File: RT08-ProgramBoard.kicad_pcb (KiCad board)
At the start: 2 copper layers, 190.5 x 149.9 mm, 313 parts, among them J1 PWR/Addr, J2 Inst-1, J3 Inst-2, J4 Data-1, J5 Data-2, J6 Inst-1, J7 Inst-2, J8 Data-1, J9 Data-2

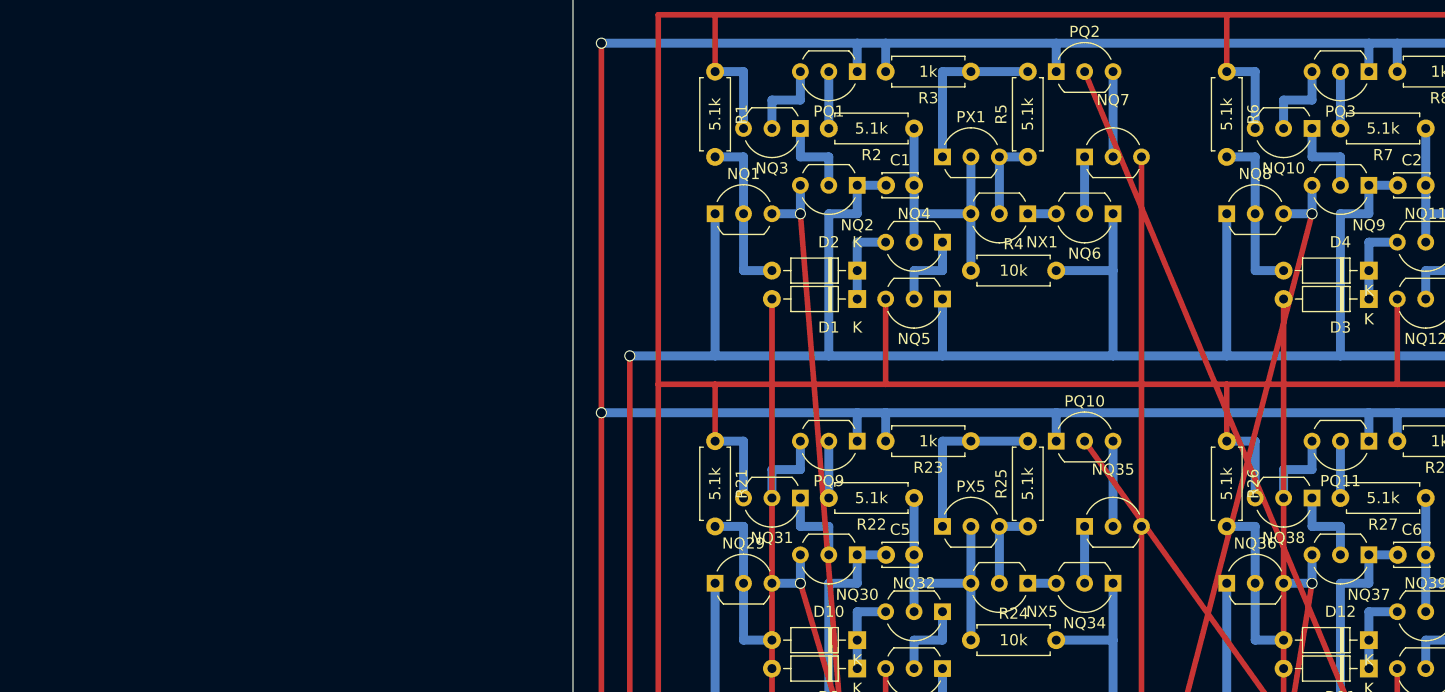
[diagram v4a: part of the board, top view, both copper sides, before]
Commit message: Adding one more parts per bit, editing PCB
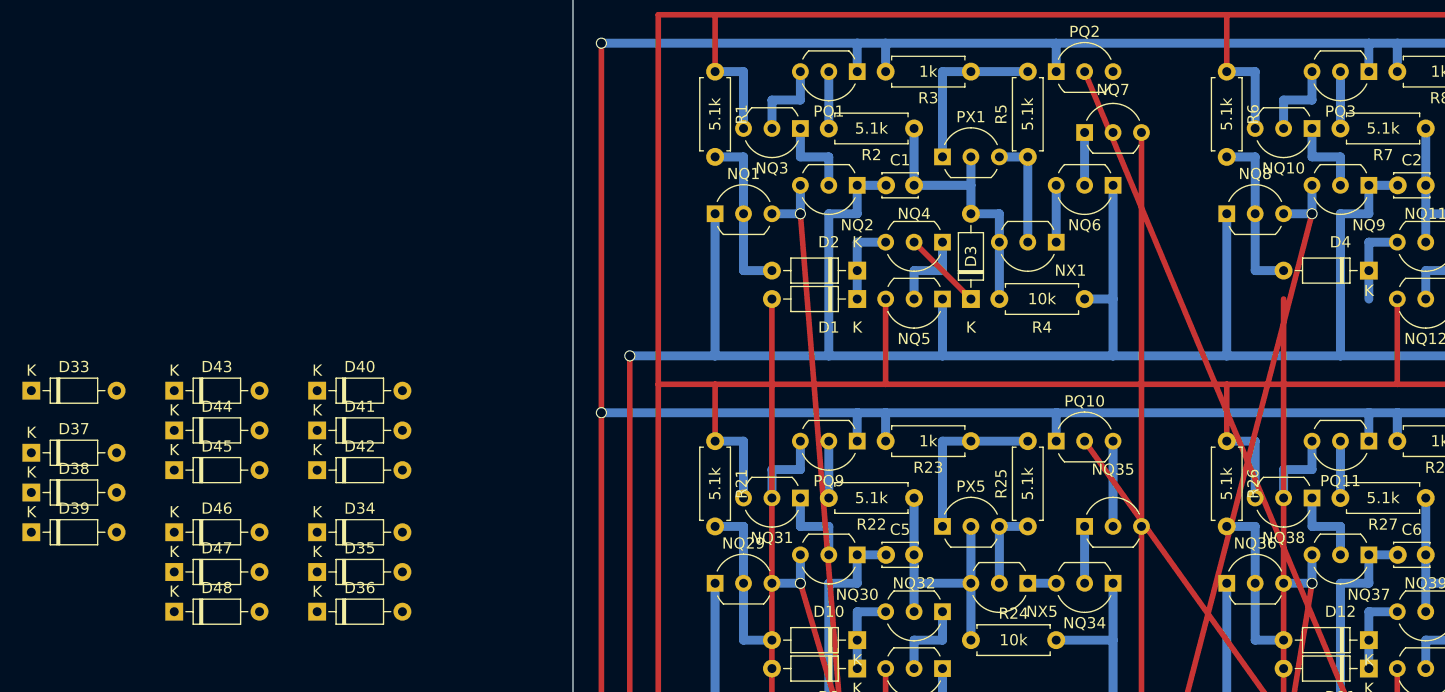
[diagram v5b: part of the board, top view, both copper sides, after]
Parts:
- added D33: Schottky, Diode_THT:D_DO-35_SOD27_P7.62mm_Horizontal, F.Cu at (-20.5, 53.9)
- added D34: Schottky, Diode_THT:D_DO-35_SOD27_P7.62mm_Horizontal, F.Cu at (5.08, 66.6)
- added D35: Schottky, Diode_THT:D_DO-35_SOD27_P7.62mm_Horizontal, F.Cu at (5.08, 70.1)
- added D36: Schottky, Diode_THT:D_DO-35_SOD27_P7.62mm_Horizontal, F.Cu at (5.08, 73.7)
- added D37: Schottky, Diode_THT:D_DO-35_SOD27_P7.62mm_Horizontal, F.Cu at (-20.5, 59.5)
- added D38: Schottky, Diode_THT:D_DO-35_SOD27_P7.62mm_Horizontal, F.Cu at (-20.5, 63.0)
- added D39: Schottky, Diode_THT:D_DO-35_SOD27_P7.62mm_Horizontal, F.Cu at (-20.5, 66.6)
- added D40: Schottky, Diode_THT:D_DO-35_SOD27_P7.62mm_Horizontal, F.Cu at (5.08, 53.9)
- added D41: Schottky, Diode_THT:D_DO-35_SOD27_P7.62mm_Horizontal, F.Cu at (5.08, 57.5)
- added D42: Schottky, Diode_THT:D_DO-35_SOD27_P7.62mm_Horizontal, F.Cu at (5.08, 61.0)
- added D43: Schottky, Diode_THT:D_DO-35_SOD27_P7.62mm_Horizontal, F.Cu at (-7.69, 53.9)
- added D44: Schottky, Diode_THT:D_DO-35_SOD27_P7.62mm_Horizontal, F.Cu at (-7.69, 57.5)
- added D45: Schottky, Diode_THT:D_DO-35_SOD27_P7.62mm_Horizontal, F.Cu at (-7.69, 61.0)
- added D46: Schottky, Diode_THT:D_DO-35_SOD27_P7.62mm_Horizontal, F.Cu at (-7.69, 66.6)
- added D47: Schottky, Diode_THT:D_DO-35_SOD27_P7.62mm_Horizontal, F.Cu at (-7.69, 70.1)
- added D48: Schottky, Diode_THT:D_DO-35_SOD27_P7.62mm_Horizontal, F.Cu at (-7.69, 73.7)
- moved D3 35.6 mm to (63.5, 45.7), turned to 90 degrees
- moved NX1 3.59 mm to (71.1, 40.6)
- moved R4 3.59 mm to (66.0, 45.7)
- moved NQ6 2.54 mm to (76.2, 35.6)
- moved NQ7 2.18 mm to (73.7, 30.8)
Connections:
- C1 pad 2: Net-(NQ4-C) -> Net-(D3-A)
- C10 pad 2: Net-(NQ67-C) -> Net-(D30-A)
- C11 pad 2: Net-(NQ74-C) -> Net-(D33-A)
- C12 pad 2: Net-(NQ81-C) -> Net-(D36-A)
- C13 pad 2: Net-(NQ88-C) -> Net-(D39-A)
- C14 pad 2: Net-(NQ95-C) -> Net-(D42-A)
- C15 pad 2: Net-(NQ102-C) -> Net-(D45-A)
- C16 pad 2: Net-(NQ109-C) -> Net-(D48-A)
- C2 pad 2: Net-(NQ11-C) -> Net-(D6-A)
- C3 pad 2: Net-(NQ18-C) -> Net-(D9-A)
- C4 pad 2: Net-(NQ25-C) -> Net-(D12-A)
- C5 pad 2: Net-(NQ32-C) -> Net-(D15-A)
- C6 pad 2: Net-(NQ39-C) -> Net-(D18-A)
- C7 pad 2: Net-(NQ46-C) -> Net-(D21-A)
- C8 pad 2: Net-(NQ53-C) -> Net-(D24-A)
- C9 pad 2: Net-(NQ60-C) -> Net-(D27-A)
- D10 pad 2: Net-(D10-A) -> /Rst
- D11 pad 1: Net-(D11-K) -> Net-(D10-K)
- D11 pad 2: /Rst -> Net-(D11-A)
- D12 pad 1: Net-(D11-K) -> Net-(D12-K)
- D15 pad 2: /Rst -> Net-(D15-A)
- D16 pad 1: Net-(D15-K) -> Net-(D16-K)
- D16 pad 2: Net-(D16-A) -> /Rst
- D17 pad 1: Net-(D17-K) -> Net-(D16-K)
- D17 pad 2: /Rst -> Net-(D17-A)
- D18 pad 1: Net-(D17-K) -> Net-(D18-K)
- D21 pad 2: /Rst -> Net-(D21-A)
- D22 pad 1: Net-(D21-K) -> Net-(D22-K)
- D22 pad 2: Net-(D22-A) -> /Rst
- D23 pad 1: Net-(D23-K) -> Net-(D22-K)
- D23 pad 2: /Rst -> Net-(D23-A)
- D24 pad 1: Net-(D23-K) -> Net-(D24-K)
- D27 pad 2: /Rst -> Net-(D27-A)
- D28 pad 1: Net-(D27-K) -> Net-(D28-K)
- D28 pad 2: Net-(D28-A) -> /Rst
- D29 pad 1: Net-(D29-K) -> Net-(D28-K)
- D29 pad 2: /Rst -> Net-(D29-A)
- D3 pad 2: /Rst -> Net-(D3-A)
- D30 pad 1: Net-(D29-K) -> Net-(D30-K)
- D4 pad 1: Net-(D3-K) -> Net-(D4-K)
- D4 pad 2: Net-(D4-A) -> /Rst
- D5 pad 1: Net-(D5-K) -> Net-(D4-K)
- D5 pad 2: /Rst -> Net-(D5-A)
- D6 pad 1: Net-(D5-K) -> Net-(D6-K)
- D9 pad 1: Net-(D10-K) -> Net-(D9-K)
- D9 pad 2: /Rst -> Net-(D9-A)
- NQ102 pad 2: Net-(NQ102-C) -> Net-(D45-K)
- NQ102 pad 3: Net-(D29-K) -> Net-(D43-K)
- NQ106 pad 2: Net-(D32-A) -> Net-(D47-A)
- NQ109 pad 2: Net-(NQ109-C) -> Net-(D48-K)
- NQ109 pad 3: Net-(D31-K) -> Net-(D46-K)
- NQ11 pad 2: Net-(NQ11-C) -> Net-(D6-K)
- NQ11 pad 3: Net-(D3-K) -> Net-(D4-K)
- NQ15 pad 2: Net-(D6-A) -> Net-(D8-A)
- NQ18 pad 2: Net-(NQ18-C) -> Net-(D9-K)
- NQ18 pad 3: Net-(D5-K) -> Net-(D7-K)
- NQ22 pad 2: Net-(D8-A) -> Net-(D11-A)
- NQ25 pad 2: Net-(NQ25-C) -> Net-(D12-K)
- NQ25 pad 3: Net-(D7-K) -> Net-(D10-K)
- NQ29 pad 2: Net-(D10-A) -> Net-(D14-A)
- NQ32 pad 2: Net-(NQ32-C) -> Net-(D15-K)
- NQ32 pad 3: Net-(D10-K) -> Net-(D13-K)
- NQ36 pad 2: Net-(D12-A) -> Net-(D17-A)
- NQ39 pad 2: Net-(NQ39-C) -> Net-(D18-K)
- NQ39 pad 3: Net-(D11-K) -> Net-(D16-K)
- NQ4 pad 2: Net-(NQ4-C) -> Net-(D3-K)
- NQ43 pad 2: Net-(D14-A) -> Net-(D20-A)
- NQ46 pad 2: Net-(NQ46-C) -> Net-(D21-K)
- NQ46 pad 3: Net-(D13-K) -> Net-(D19-K)
- NQ50 pad 2: Net-(D16-A) -> Net-(D23-A)
- NQ53 pad 2: Net-(NQ53-C) -> Net-(D24-K)
- NQ53 pad 3: Net-(D15-K) -> Net-(D22-K)
- NQ57 pad 2: Net-(D18-A) -> Net-(D26-A)
- NQ60 pad 2: Net-(NQ60-C) -> Net-(D27-K)
- NQ60 pad 3: Net-(D17-K) -> Net-(D25-K)
- NQ64 pad 2: Net-(D20-A) -> Net-(D29-A)
- NQ67 pad 2: Net-(NQ67-C) -> Net-(D30-K)
- NQ67 pad 3: Net-(D19-K) -> Net-(D28-K)
- NQ71 pad 2: Net-(D22-A) -> Net-(D32-A)
- NQ74 pad 2: Net-(NQ74-C) -> Net-(D33-K)
- NQ74 pad 3: Net-(D21-K) -> Net-(D31-K)
- NQ78 pad 2: Net-(D24-A) -> Net-(D35-A)
- NQ8 pad 2: Net-(D4-A) -> Net-(D5-A)
- NQ81 pad 2: Net-(NQ81-C) -> Net-(D36-K)
- NQ81 pad 3: Net-(D23-K) -> Net-(D34-K)
- NQ85 pad 2: Net-(D26-A) -> Net-(D38-A)
- NQ88 pad 2: Net-(NQ88-C) -> Net-(D39-K)
- NQ88 pad 3: Net-(D25-K) -> Net-(D37-K)
- NQ92 pad 2: Net-(D28-A) -> Net-(D41-A)
- NQ95 pad 2: Net-(NQ95-C) -> Net-(D42-K)
- NQ95 pad 3: Net-(D27-K) -> Net-(D40-K)
- NQ99 pad 2: Net-(D30-A) -> Net-(D44-A)
- NX1 pad 3: Net-(NQ4-C) -> Net-(D3-A)
- NX10 pad 3: Net-(NQ67-C) -> Net-(D30-A)
- NX11 pad 3: Net-(NQ74-C) -> Net-(D33-A)
- NX12 pad 3: Net-(NQ81-C) -> Net-(D36-A)
- NX13 pad 3: Net-(NQ88-C) -> Net-(D39-A)
- NX14 pad 3: Net-(NQ95-C) -> Net-(D42-A)
- NX15 pad 3: Net-(NQ102-C) -> Net-(D45-A)
- NX16 pad 3: Net-(NQ109-C) -> Net-(D48-A)
- NX2 pad 3: Net-(NQ11-C) -> Net-(D6-A)
- NX3 pad 3: Net-(NQ18-C) -> Net-(D9-A)
- NX4 pad 3: Net-(NQ25-C) -> Net-(D12-A)
- NX5 pad 3: Net-(NQ32-C) -> Net-(D15-A)
- NX6 pad 3: Net-(NQ39-C) -> Net-(D18-A)
- NX7 pad 3: Net-(NQ46-C) -> Net-(D21-A)
- NX8 pad 3: Net-(NQ53-C) -> Net-(D24-A)
- NX9 pad 3: Net-(NQ60-C) -> Net-(D27-A)
- PX1 pad 2: Net-(NQ4-C) -> Net-(D3-A)
- PX10 pad 2: Net-(NQ67-C) -> Net-(D30-A)
- PX11 pad 2: Net-(NQ74-C) -> Net-(D33-A)
- PX12 pad 2: Net-(NQ81-C) -> Net-(D36-A)
- PX13 pad 2: Net-(NQ88-C) -> Net-(D39-A)
- PX14 pad 2: Net-(NQ95-C) -> Net-(D42-A)
- PX15 pad 2: Net-(NQ102-C) -> Net-(D45-A)
- PX16 pad 2: Net-(NQ109-C) -> Net-(D48-A)
- PX2 pad 2: Net-(NQ11-C) -> Net-(D6-A)
- PX3 pad 2: Net-(NQ18-C) -> Net-(D9-A)
- PX4 pad 2: Net-(NQ25-C) -> Net-(D12-A)
- PX5 pad 2: Net-(NQ32-C) -> Net-(D15-A)
- PX6 pad 2: Net-(NQ39-C) -> Net-(D18-A)
- PX7 pad 2: Net-(NQ46-C) -> Net-(D21-A)
- PX8 pad 2: Net-(NQ53-C) -> Net-(D24-A)
- PX9 pad 2: Net-(NQ60-C) -> Net-(D27-A)
- R11 pad 2: Net-(D6-A) -> Net-(D8-A)
- R12 pad 1: Net-(NQ18-C) -> Net-(D9-A)
- R14 pad 1: Net-(NQ18-C) -> Net-(D9-A)
- R16 pad 2: Net-(D8-A) -> Net-(D11-A)
- R17 pad 1: Net-(NQ25-C) -> Net-(D12-A)
- R19 pad 1: Net-(NQ25-C) -> Net-(D12-A)
- R2 pad 1: Net-(NQ4-C) -> Net-(D3-A)
- R21 pad 2: Net-(D10-A) -> Net-(D14-A)
- R22 pad 1: Net-(NQ32-C) -> Net-(D15-A)
- R24 pad 1: Net-(NQ32-C) -> Net-(D15-A)
- R26 pad 2: Net-(D12-A) -> Net-(D17-A)
- R27 pad 1: Net-(NQ39-C) -> Net-(D18-A)
- R29 pad 1: Net-(NQ39-C) -> Net-(D18-A)
- R31 pad 2: Net-(D14-A) -> Net-(D20-A)
- R32 pad 1: Net-(NQ46-C) -> Net-(D21-A)
- R34 pad 1: Net-(NQ46-C) -> Net-(D21-A)
- R36 pad 2: Net-(D16-A) -> Net-(D23-A)
- R37 pad 1: Net-(NQ53-C) -> Net-(D24-A)
- R39 pad 1: Net-(NQ53-C) -> Net-(D24-A)
- R4 pad 1: Net-(NQ4-C) -> Net-(D3-A)
- R41 pad 2: Net-(D18-A) -> Net-(D26-A)
- R42 pad 1: Net-(NQ60-C) -> Net-(D27-A)
- R44 pad 1: Net-(NQ60-C) -> Net-(D27-A)
- R46 pad 2: Net-(D20-A) -> Net-(D29-A)
- R47 pad 1: Net-(NQ67-C) -> Net-(D30-A)
- R49 pad 1: Net-(NQ67-C) -> Net-(D30-A)
- R51 pad 2: Net-(D22-A) -> Net-(D32-A)
- R52 pad 1: Net-(NQ74-C) -> Net-(D33-A)
- R54 pad 1: Net-(NQ74-C) -> Net-(D33-A)
- R56 pad 2: Net-(D24-A) -> Net-(D35-A)
- R57 pad 1: Net-(NQ81-C) -> Net-(D36-A)
- R59 pad 1: Net-(NQ81-C) -> Net-(D36-A)
- R6 pad 2: Net-(D4-A) -> Net-(D5-A)
- R61 pad 2: Net-(D26-A) -> Net-(D38-A)
- R62 pad 1: Net-(NQ88-C) -> Net-(D39-A)
- R64 pad 1: Net-(NQ88-C) -> Net-(D39-A)
- R66 pad 2: Net-(D28-A) -> Net-(D41-A)
- R67 pad 1: Net-(NQ95-C) -> Net-(D42-A)
- R69 pad 1: Net-(NQ95-C) -> Net-(D42-A)
- R7 pad 1: Net-(NQ11-C) -> Net-(D6-A)
- R71 pad 2: Net-(D30-A) -> Net-(D44-A)
- R72 pad 1: Net-(NQ102-C) -> Net-(D45-A)
- R74 pad 1: Net-(NQ102-C) -> Net-(D45-A)
- R76 pad 2: Net-(D32-A) -> Net-(D47-A)
- R77 pad 1: Net-(NQ109-C) -> Net-(D48-A)
- R79 pad 1: Net-(NQ109-C) -> Net-(D48-A)
- R9 pad 1: Net-(NQ11-C) -> Net-(D6-A)
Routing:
- net (no net): track 0.00 -> 337.8 mm
- net Net-(NQ67-C): track 25.4 -> 0.00 mm
- net Net-(NQ60-C): track 25.4 -> 0.00 mm
- net Net-(D3-A): track 0.00 -> 25.4 mm
- net Net-(NQ4-C): track 25.4 -> 0.00 mm
- net Net-(NQ11-C): track 25.4 -> 0.00 mm
- net Net-(NQ95-C): track 25.4 -> 0.00 mm
- net Net-(NQ88-C): track 25.4 -> 0.00 mm
- net Net-(NQ81-C): track 25.4 -> 0.00 mm
- net Net-(NQ74-C): track 25.4 -> 0.00 mm
- net Net-(NQ39-C): track 25.4 -> 0.00 mm
- net Net-(NQ32-C): track 25.4 -> 0.00 mm
- net Net-(D6-A): track 15.2 -> 40.6 mm
- net Net-(D18-A): track 15.2 -> 40.6 mm
- net Net-(D15-K): track 7.62 -> 33.0 mm
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
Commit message: Finished editing PCB
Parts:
- moved D48 220.2 mm to (200.7, 144.8), turned to 90 degrees
- moved D46 213.1 mm to (190.5, 144.8), turned to 180 degrees
- moved D47 210.9 mm to (190.5, 142.2), turned to 180 degrees
- moved D36 199.3 mm to (200.7, 111.8), turned to 90 degrees
- moved D34 190.8 mm to (190.5, 111.8), turned to 180 degrees
- moved D35 189.5 mm to (190.5, 109.2), turned to 180 degrees
- moved D33 184.7 mm to (154.9, 111.8), turned to 90 degrees
- moved D45 182.9 mm to (154.9, 144.8), turned to 90 degrees
- moved D43 177.5 mm to (144.8, 144.8), turned to 180 degrees
- moved D44 174.5 mm to (144.8, 142.2), turned to 180 degrees
- moved D10 140.5 mm to (190.5, 45.7)
- moved D42 133.7 mm to (109.2, 144.8), turned to 90 degrees
- moved D40 130.7 mm to (99.1, 144.8), turned to 180 degrees
- moved D15 127.0 mm to (63.5, 78.7), turned to 90 degrees
- moved D41 126.6 mm to (99.1, 142.2), turned to 180 degrees
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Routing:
- net (no net): track 337.8 -> 0.00 mm
- net Net-(D15-K): track 33.0 -> 0.00 mm
- net Net-(D42-A): track 0.00 -> 25.4 mm
- net Net-(D39-A): track 0.00 -> 25.4 mm
- net Net-(D27-A): track 0.00 -> 25.4 mm
- net Net-(D15-A): track 0.00 -> 25.4 mm
- net Net-(D48-A): track 0.00 -> 25.4 mm
- net Net-(D45-A): track 0.00 -> 25.4 mm
- net Net-(D36-A): track 0.00 -> 25.4 mm
- net Net-(D33-A): track 0.00 -> 25.4 mm
- net Net-(D9-A): track 0.00 -> 25.4 mm
- net Net-(D21-A): track 0.00 -> 25.4 mm
- net Net-(D12-A): track 40.6 -> 25.4 mm
- net Net-(D5-A): track 0.00 -> 15.2 mm
- net Net-(D41-A): track 0.00 -> 15.2 mm
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
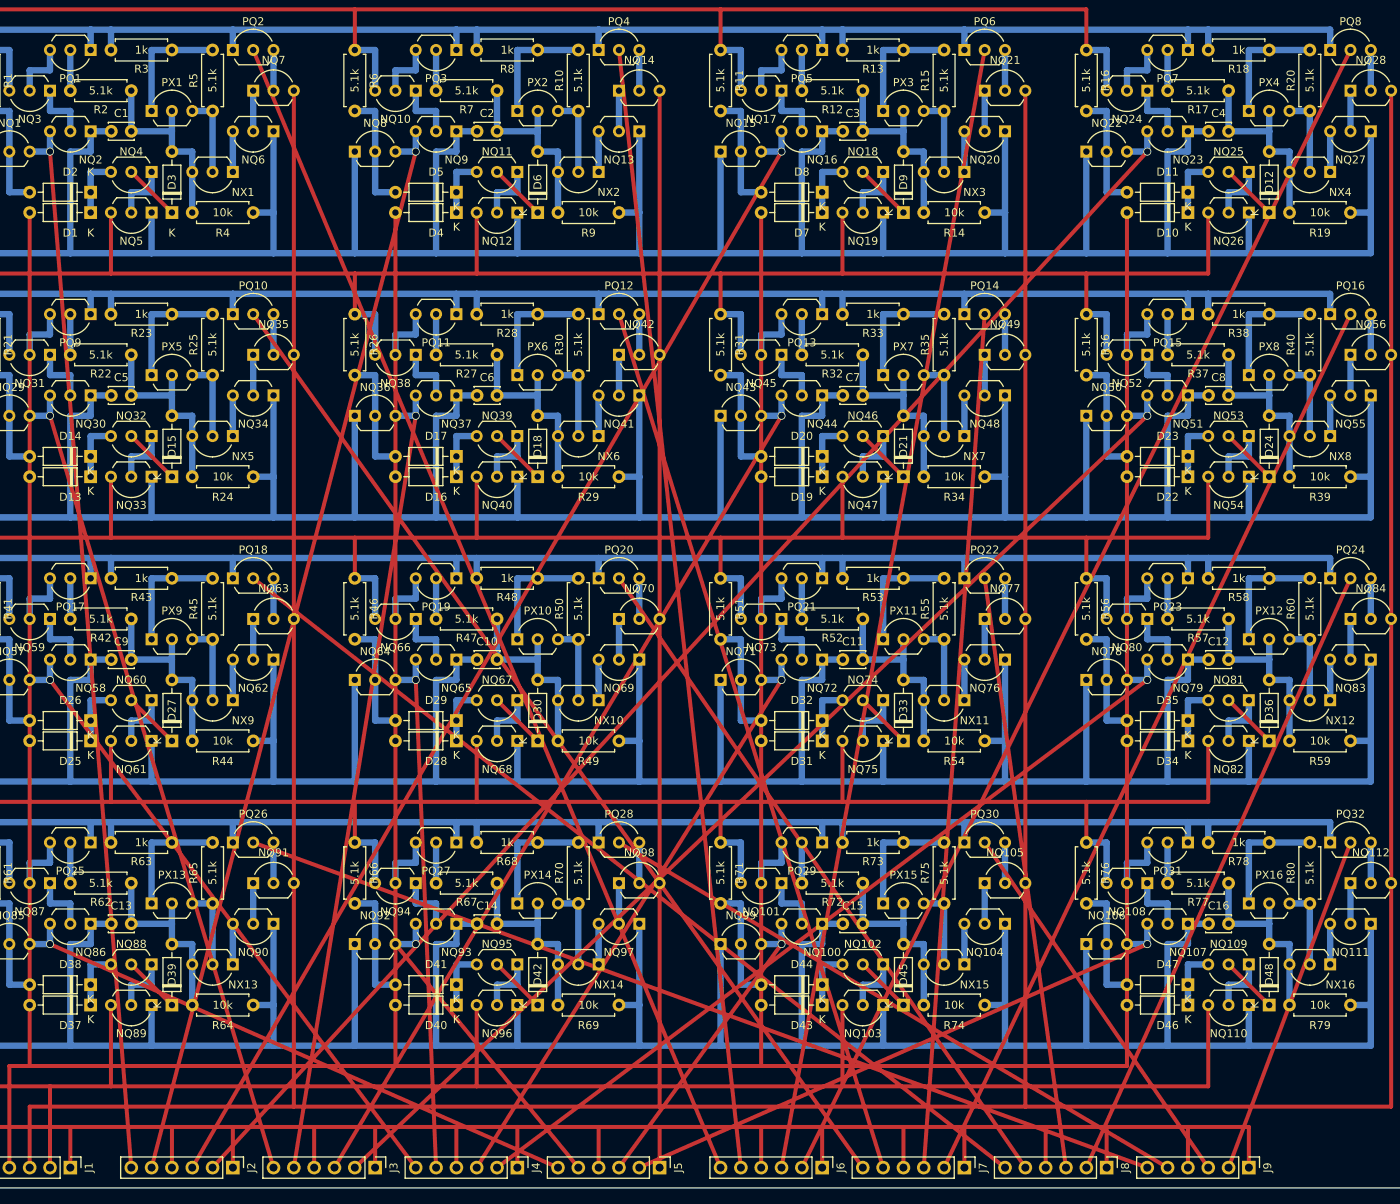
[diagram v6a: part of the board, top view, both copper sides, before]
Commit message: Merged In/Out pins to one pin groups!
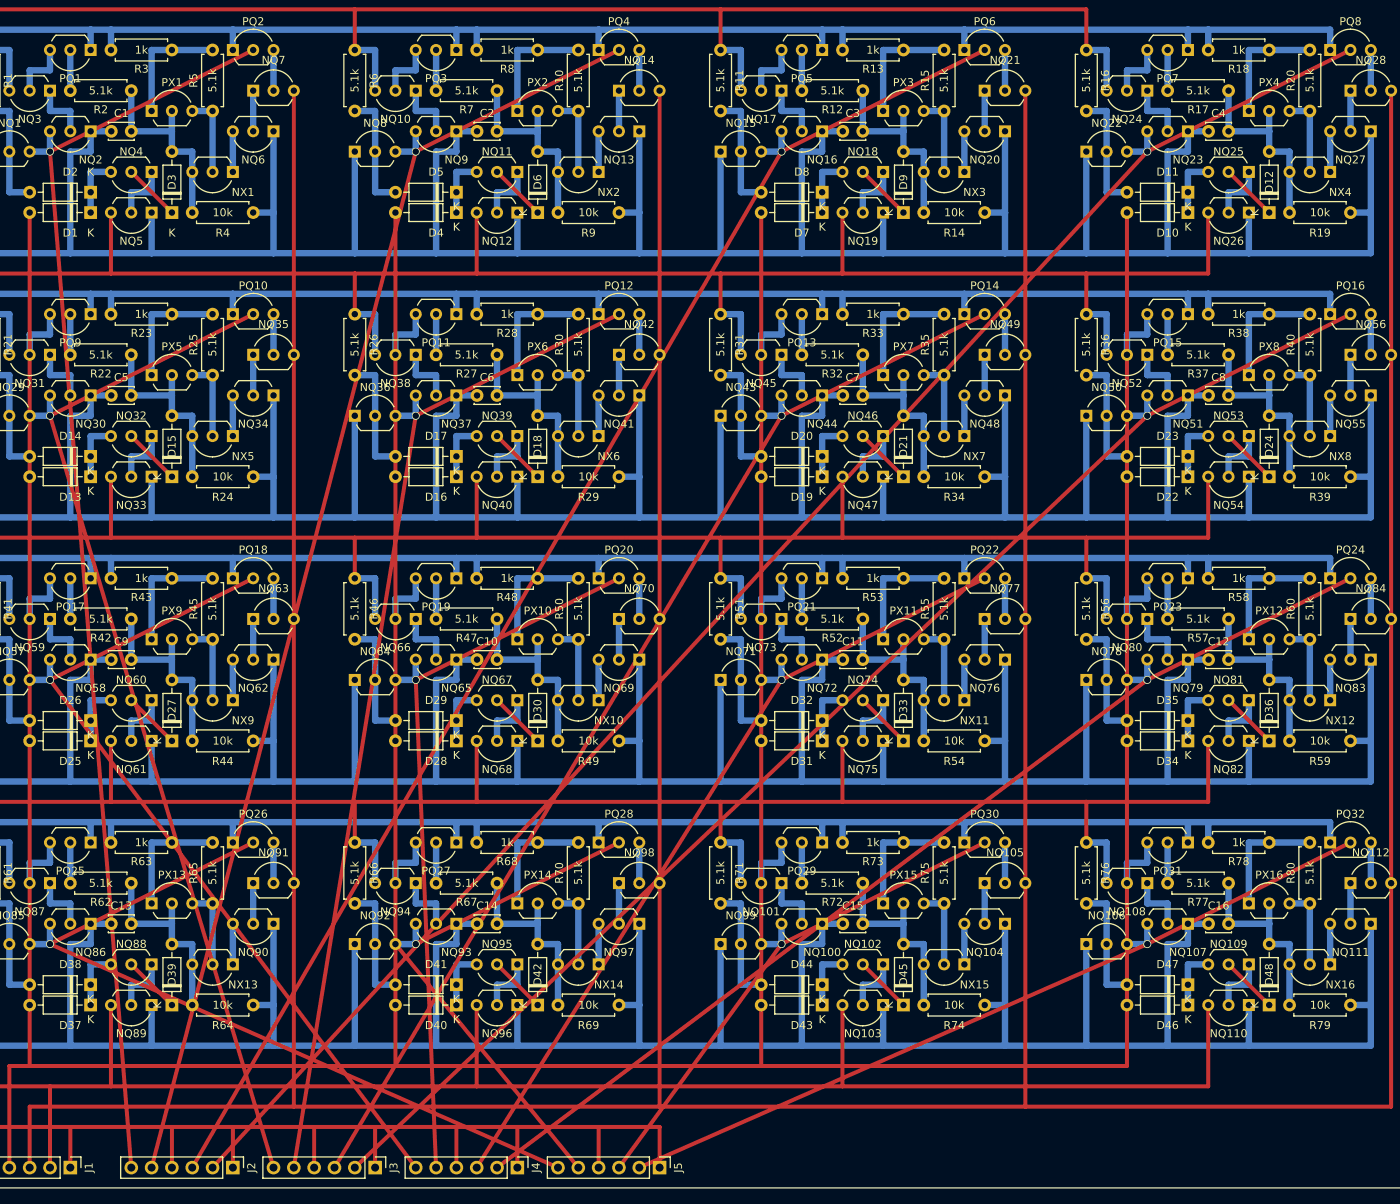
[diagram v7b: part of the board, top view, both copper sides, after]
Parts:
- removed J6: Inst-1, Connector_PinHeader_2.54mm:PinHeader_1x06_P2.54mm_Vertical
- removed J7: Inst-2, Connector_PinHeader_2.54mm:PinHeader_1x06_P2.54mm_Vertical
- removed J8: Data-1, Connector_PinHeader_2.54mm:PinHeader_1x06_P2.54mm_Vertical
- removed J9: Data-2, Connector_PinHeader_2.54mm:PinHeader_1x06_P2.54mm_Vertical
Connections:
- PQ10 pad 2: /P4 -> /D4
- PQ12 pad 2: /P5 -> /D5
- PQ14 pad 2: /P6 -> /D6
- PQ16 pad 2: /P7 -> /D7
- PQ18 pad 2: /P8 -> /D8
- PQ2 pad 2: /P0 -> /D0
- PQ20 pad 2: /P9 -> /D9
- PQ22 pad 2: /P10 -> /D10
- PQ24 pad 2: /P11 -> /D11
- PQ26 pad 2: /P12 -> /D12
- PQ28 pad 2: /P13 -> /D13
- PQ30 pad 2: /P14 -> /D14
- PQ32 pad 2: /P15 -> /D15
- PQ4 pad 2: /P1 -> /D1
- PQ6 pad 2: /P2 -> /D2
- PQ8 pad 2: /P3 -> /D3
